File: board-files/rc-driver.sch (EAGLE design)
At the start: 13 parts, among them IC1 TINY22S

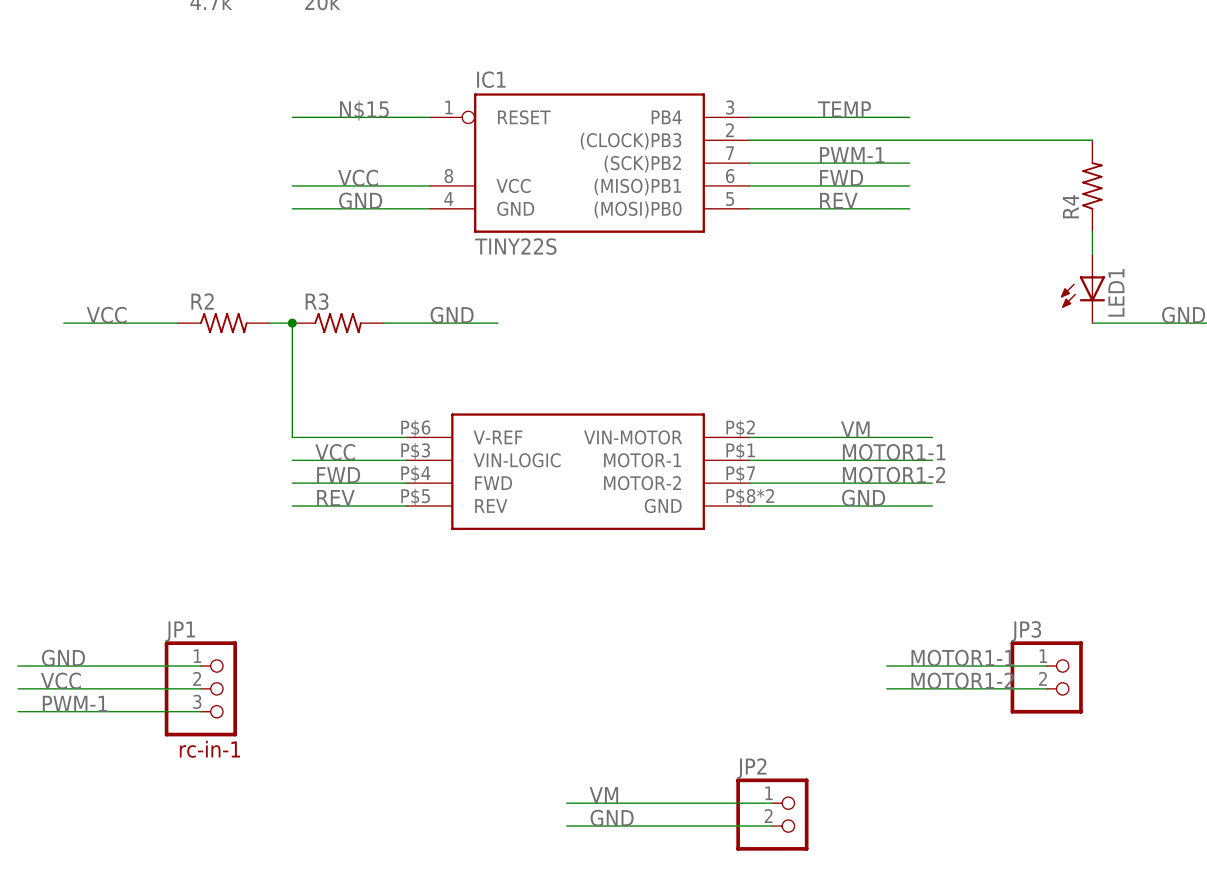
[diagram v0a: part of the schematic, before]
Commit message: Added start os v 2.0 files. Need to connect vref.
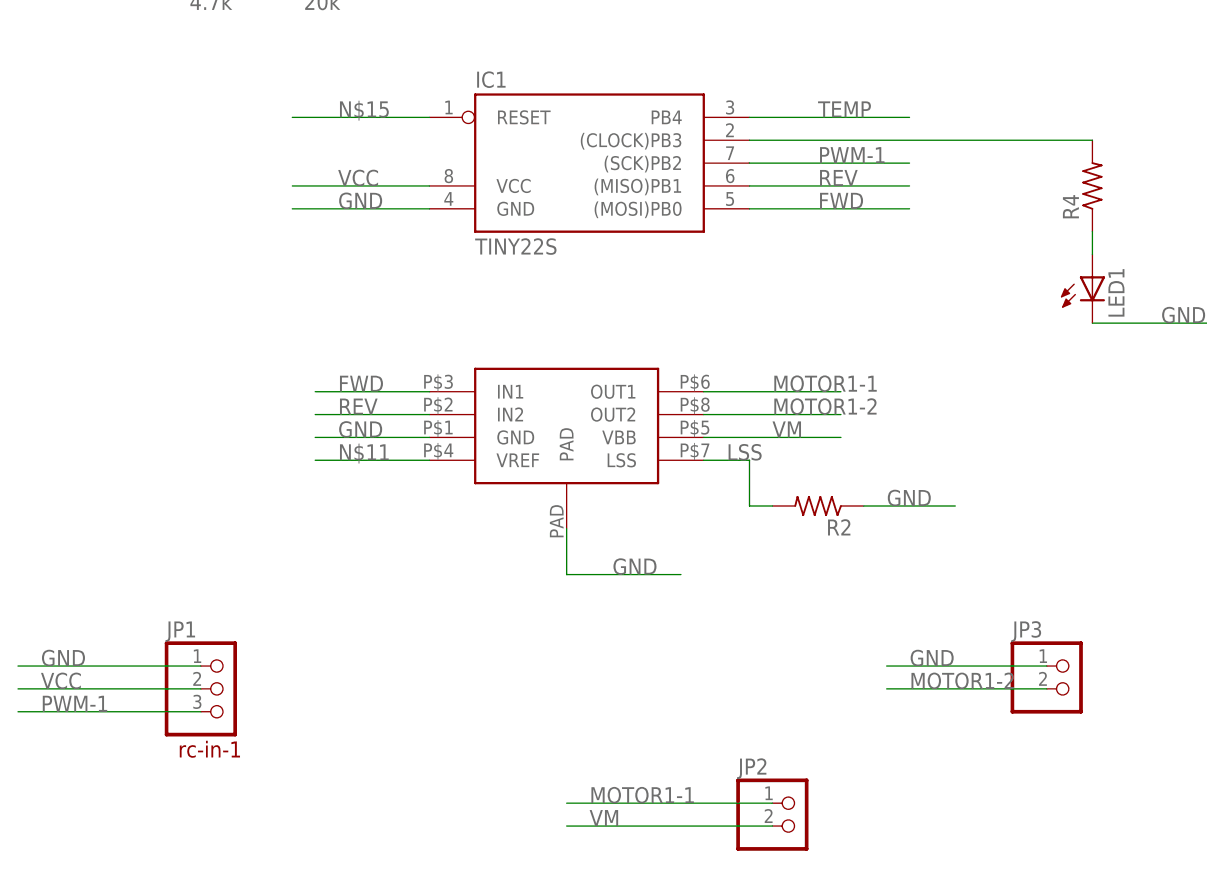
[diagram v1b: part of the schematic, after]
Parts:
- removed R3: (no value), resistor:R-US_R0603
- R2: device resistor:R-US_R0603 -> resistor:R-US_R0805W
- U$1: value ZXBM5210-MOTOR-DRIVER -> A4950-HBRIDGE; device mgregg:ZXBM5210-MOTOR-DRIVER -> mgregg:A4950-HBRIDGE
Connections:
- removed net N$1: R2.2, R3.1, U$1.V-REF
- new net LSS: R2.2, U$1.LSS
- new net N$11: U$1.VREF
- net FWD: now also IC1.(MOSI)PB0, U$1.IN1; no longer IC1.(MISO)PB1, U$1.FWD
- net GND: now also JP3.1, R2.1, U$1.PAD; no longer JP2.2, R3.2
- net MOTOR1-1: now also JP2.1, U$1.OUT1; no longer JP3.1, U$1.MOTOR-1
- net MOTOR1-2: now also U$1.OUT2; no longer U$1.MOTOR-2
- net REV: now also IC1.(MISO)PB1, U$1.IN2; no longer IC1.(MOSI)PB0, U$1.REV
- net VCC: no longer R2.1, U$1.VIN-LOGIC
- net VM: now also JP2.2, U$1.VBB; no longer JP2.1, U$1.VIN-MOTOR
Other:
- moved on the sheet: R2

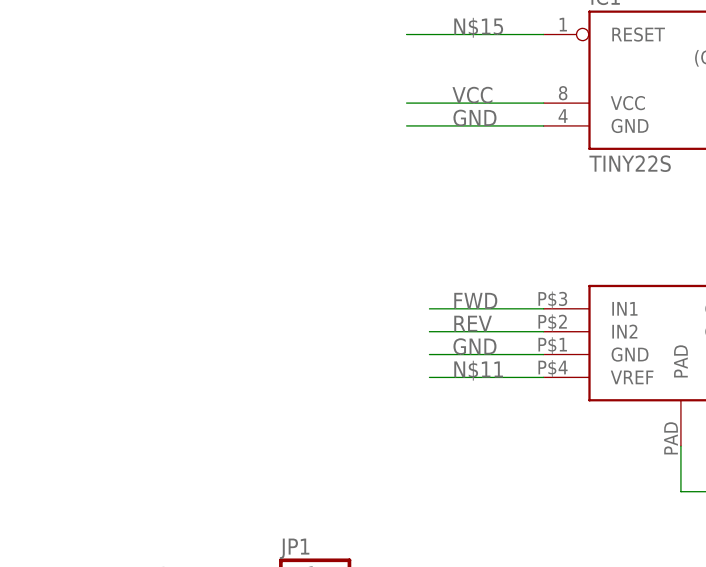
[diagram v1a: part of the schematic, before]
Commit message: Adding RC net to VREF. Creating gerbers for plain board.
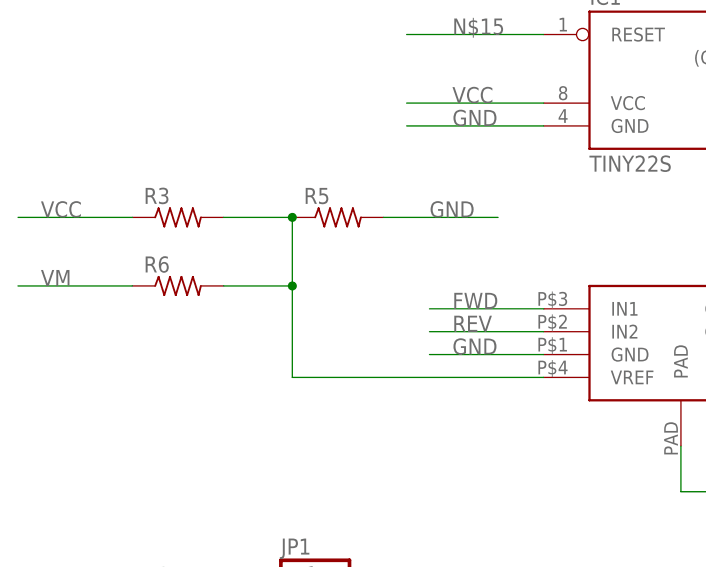
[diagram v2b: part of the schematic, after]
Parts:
- added R3, R5, R6: (no value), resistor:R-US_R0603
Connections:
- removed net N$11: U$1.VREF
- new net N$1: R3.2, R5.1, R6.2, U$1.VREF
- net GND: now also R5.2
- net VCC: now also R3.1
- net VM: now also R6.1
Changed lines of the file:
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@@
 <part name="U$1" library="mgregg" deviceset="A4950-HBRIDGE" device=""/>
 <part name="R2" library="resistor" deviceset="R-US_" device="R0805W"/>
+<part name="R3" library="resistor" deviceset="R-US_" device="R0603"/>
+<part name="R5" library="resistor" deviceset="R-US_" device="R0603"/>
+<part name="R6" library="resistor" deviceset="R-US_" device="R0603"/>
 </parts>
 <sheets>
@@
 <instance part="U$1" gate="G$1" x="0" y="22.86"/>
 <instance part="R2" gate="G$1" x="25.4" y="17.78" rot="R180"/>
+<instance part="R3" gate="G$1" x="-58.42" y="40.64"/>
+<instance part="R5" gate="G$1" x="-40.64" y="40.64"/>
+<instance part="R6" gate="G$1" x="-58.42" y="33.02"/>
 </instances>
 <busses>
@@
 <label x="35.56" y="0" size="1.778" layer="95"/>
 </segment>
+<segment>
+<pinref part="R5" gate="G$1" pin="2"/>
+<wire x1="-35.56" y1="40.64" x2="-22.86" y2="40.64" width="0.1524" layer="91"/>
+<label x="-30.48" y="40.64" size="1.778" layer="95"/>
+</segment>
 </net>
 <net name="VM" class="0">
@@
 <label x="0" y="-17.78" size="1.778" layer="95"/>
 </segment>
+<segment>
+<pinref part="R6" gate="G$1" pin="1"/>
+<wire x1="-63.5" y1="33.02" x2="-76.2" y2="33.02" width="0.1524" layer="91"/>
+<label x="-73.66" y="33.02" size="1.778" layer="95"/>
+</segment>
 </net>
 <net name="VCC" class="0">
@@
 <wire x1="-45.72" y1="76.2" x2="-55.88" y2="76.2" width="0.1524" layer="91"/>
 <label x="-53.34" y="76.2" size="1.778" layer="95"/>
+</segment>
+<segment>
+<pinref part="R3" gate="G$1" pin="1"/>
+<wire x1="-63.5" y1="40.64" x2="-76.2" y2="40.64" width="0.1524" layer="91"/>
+<label x="-73.66" y="40.64" size="1.778" layer="95"/>
 </segment>
 </net>
@@
 </segment>
 </net>
-<net name="N$11" class="0">
-<segment>
-<pinref part="U$1" gate="G$1" pin="VREF"/>
-<wire x1="-17.78" y1="22.86" x2="-30.48" y2="22.86" width="0.1524" layer="91"/>
-<label x="-27.94" y="22.86" size="1.778" layer="95"/>
-</segment>
-</net>
 <net name="LSS" class="0">
 <segment>
@@
 </segment>
 </net>
+<net name="N$1" class="0">
+<segment>
+<pinref part="R3" gate="G$1" pin="2"/>
+<pinref part="R5" gate="G$1" pin="1"/>
+<wire x1="-53.34" y1="40.64" x2="-45.72" y2="40.64" width="0.1524" layer="91"/>
+<wire x1="-45.72" y1="40.64" x2="-45.72" y2="33.02" width="0.1524" layer="91"/>
+<pinref part="U$1" gate="G$1" pin="VREF"/>
+<wire x1="-45.72" y1="33.02" x2="-45.72" y2="22.86" width="0.1524" layer="91"/>
+<wire x1="-45.72" y1="22.86" x2="-17.78" y2="22.86" width="0.1524" layer="91"/>
+<junction x="-45.72" y="40.64"/>
+<pinref part="R6" gate="G$1" pin="2"/>
+<wire x1="-53.34" y1="33.02" x2="-45.72" y2="33.02" width="0.1524" layer="91"/>
+<junction x="-45.72" y="33.02"/>
+</segment>
+</net>

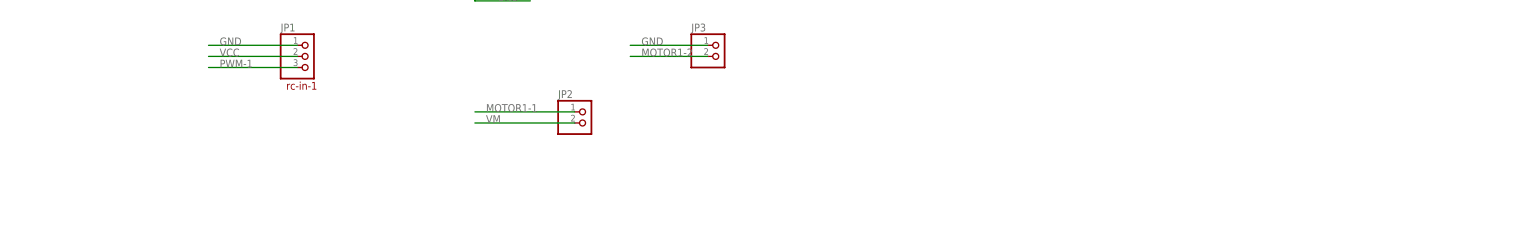
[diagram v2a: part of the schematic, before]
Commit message: Added license to boards. Finished routingand silks.
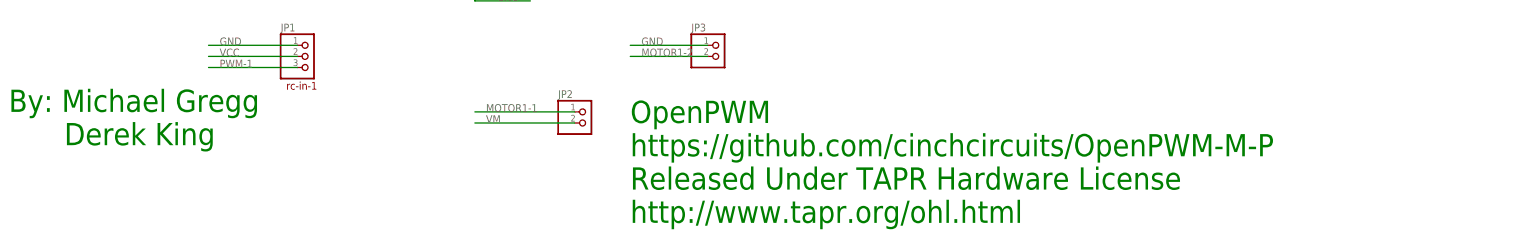
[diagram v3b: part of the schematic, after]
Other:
- note added: "By: Michael Gregg"
- note added: "Derek King"
- note added: "OpenPWM"
- note added: "Released Under TAPR Hardware License"
- note added: "http://www.tapr.org/ohl.html"
- note added: "https://github.com/cinchcircuits/OpenPWM-M-P"
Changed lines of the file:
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@@
 <?xml version="1.0" encoding="utf-8"?>
 <!DOCTYPE eagle SYSTEM "eagle.dtd">
-<eagle version="7.1.0">
+<eagle version="7.2.0">
 <drawing>
 <settings>
@@
 <plain>
 <text x="-45.72" y="-10.16" size="1.778" layer="94">rc-in-1</text>
+<text x="-109.22" y="-15.24" size="5.08" layer="91" ratio="17">By: Michael Gregg</text>
+<text x="-96.52" y="-22.86" size="5.08" layer="91" ratio="17">Derek King</text>
+<text x="33.02" y="-17.78" size="5.08" layer="91" ratio="17">OpenPWM</text>
+<text x="33.02" y="-25.4" size="5.08" layer="91" ratio="17">https://github.com/cinchcircuits/OpenPWM-M-P</text>
+<text x="33.02" y="-33.02" size="5.08" layer="91" ratio="17">Released Under TAPR Hardware License</text>
+<text x="33.02" y="-40.64" size="5.08" layer="91" ratio="17">http://www.tapr.org/ohl.html</text>
 </plain>
 <instances>

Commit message: Moving single board files to different folder.
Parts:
- R3: value (none) -> 5600
- R5: value (none) -> 1300
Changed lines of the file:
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@@
 <part name="U$1" library="mgregg" deviceset="A4950-HBRIDGE" device=""/>
 <part name="R2" library="resistor" deviceset="R-US_" device="R0805W"/>
-<part name="R3" library="resistor" deviceset="R-US_" device="R0603"/>
-<part name="R5" library="resistor" deviceset="R-US_" device="R0603"/>
+<part name="R3" library="resistor" deviceset="R-US_" device="R0603" value="5600"/>
+<part name="R5" library="resistor" deviceset="R-US_" device="R0603" value="1300"/>
 <part name="R6" library="resistor" deviceset="R-US_" device="R0603"/>
 </parts>
